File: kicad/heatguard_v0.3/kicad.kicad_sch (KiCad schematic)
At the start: 31 parts, among them J1 Conn_02x02_Odd_Even, J20 Conn_01x01, J7 Conn_01x12, J8 Conn_02x04_Odd_Even, J9 Conn_02x04_Odd_Even, U1 LM75B, U2 LM75B, U3 M24C02-FMN, U4 XIAO-RP2040-DIP

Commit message: Changes v0.2 -> v0.3 A
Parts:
- added Logo_open_hardware101: Logo_Open_Hardware_Small, Symbol:OSHW-Logo2_9.8x8mm_SilkScreen, symbol Graphic:Logo_Open_Hardware_Small
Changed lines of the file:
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@@
+	)
+	(symbol
+		(lib_id "Graphic:Logo_Open_Hardware_Small")
+		(at 182.88 261.62 0)
+		(unit 1)
+		(exclude_from_sim no)
+		(in_bom no)
+		(on_board yes)
+		(dnp no)
+		(fields_autoplaced yes)
+		(property "Reference" "Logo_open_hardware101"
+			(at 182.88 254.635 0)
+			(effects
+				(font
+					(size 1.27 1.27)
+				)
+				(hide yes)
+			)
+		)
+		(property "Value" "Logo_Open_Hardware_Small"
+			(at 182.88 267.335 0)
+			(effects
+				(font
+					(size 1.27 1.27)
+				)
+				(hide yes)
+			)
+		)
+		(property "Footprint" "Symbol:OSHW-Logo2_9.8x8mm_SilkScreen"
+			(at 182.88 261.62 0)
+			(effects
+				(font
+					(size 1.27 1.27)
+				)
+				(hide yes)
+			)
+		)
+		(property "Datasheet" "~"
+			(at 182.88 261.62 0)
+			(effects
+				(font
+					(size 1.27 1.27)
+				)
+				(hide yes)
+			)
+		)
+		(property "Description" "Open Hardware logo, small"
+			(at 182.88 261.62 0)
+			(effects
+				(font
+					(size 1.27 1.27)
+				)
+				(hide yes)
+			)
+		)
+		(instances
+			(project "kicad"
+				(path "/35c47459-45a7-4753-acae-c8b47e7575e1"
+					(reference "Logo_open_hardware101")
+					(unit 1)
+				)
+			)
+		)
 	)
 	(symbol

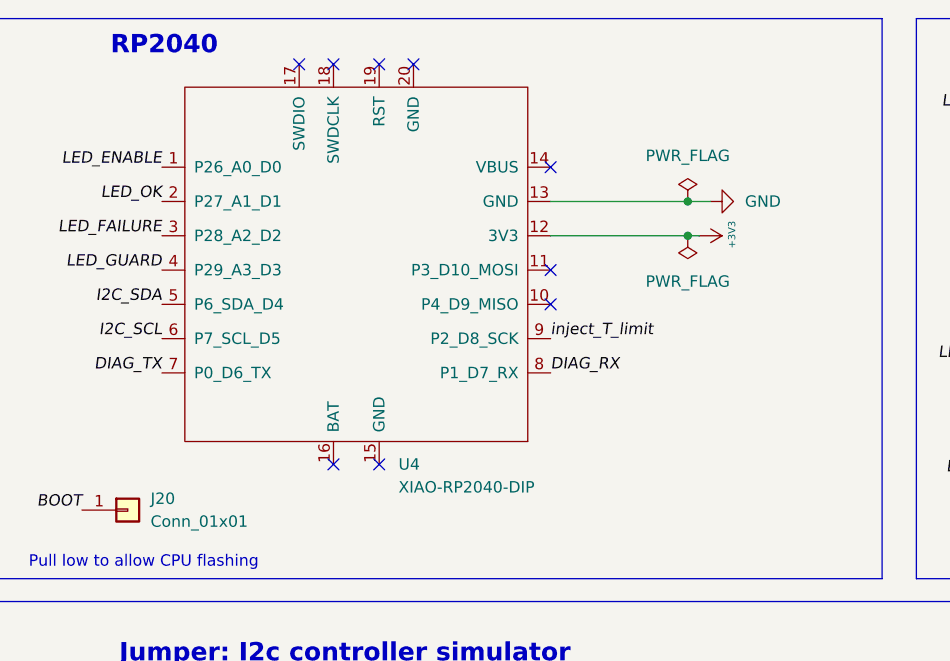
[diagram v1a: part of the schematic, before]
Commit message: Changes v0.2 -> v0.3 B: PCB: XIAO rp2040: Replace SMD with THT
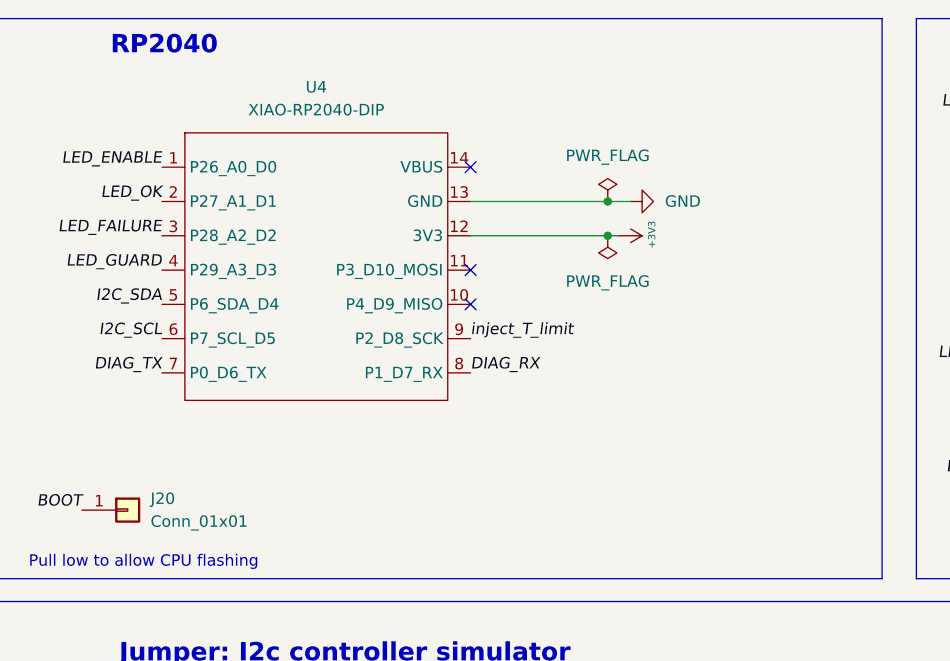
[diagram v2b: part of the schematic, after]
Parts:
- U4: footprint 00_project_library:XIAO-RP2040-SMD -> 00_project_library:XIAO-RP2040-DIP; symbol 00_project_library:XIAO-RP2040-SMD -> 00_project_library:XIAO-RP2040-DIP; now in the parts list
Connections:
- no-connect marks 18 -> 12
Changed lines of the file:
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@@
 	)
 	(junction
-		(at 99.06 39.37)
+		(at 90.17 39.37)
 		(diameter 0)
 		(color 0 0 0 0)
@@
 	)
 	(junction
-		(at 99.06 35.56)
+		(at 90.17 35.56)
 		(diameter 0)
 		(color 0 0 0 0)
@@
 	)
 	(no_connect
-		(at 83.82 43.18)
+		(at 74.93 43.18)
 	)
 	(no_connect
@@
 	)
 	(no_connect
-		(at 59.69 20.32)
-	)
-	(no_connect
 		(at 104.14 245.11)
 	)
@@
 	)
 	(no_connect
-		(at 64.77 64.77)
-	)
-	(no_connect
-		(at 68.58 20.32)
-	)
-	(no_connect
-		(at 59.69 64.77)
-	)
-	(no_connect
-		(at 55.88 20.32)
-	)
-	(no_connect
 		(at 104.14 240.03)
 	)
 	(no_connect
-		(at 83.82 31.75)
+		(at 74.93 31.75)
 	)
 	(no_connect
-		(at 83.82 46.99)
+		(at 74.93 46.99)
 	)
 	(no_connect
@@
 	)
 	(no_connect
-		(at 64.77 20.32)
-	)
-	(no_connect
 		(at 104.14 237.49)
 	)
@@
 	(wire
 		(pts
-			(xy 83.82 35.56) (xy 99.06 35.56)
+			(xy 74.93 35.56) (xy 90.17 35.56)
 		)
 		(stroke
@@
 	(wire
 		(pts
-			(xy 101.6 35.56) (xy 99.06 35.56)
+			(xy 92.71 35.56) (xy 90.17 35.56)
 		)
 		(stroke
@@
 	(wire
 		(pts
-			(xy 100.33 39.37) (xy 99.06 39.37)
+			(xy 91.44 39.37) (xy 90.17 39.37)
 		)
 		(stroke
@@
 	(wire
 		(pts
-			(xy 83.82 39.37) (xy 99.06 39.37)
+			(xy 74.93 39.37) (xy 90.17 39.37)
 		)
 		(stroke
@@
 	)
 	(label "inject_T_limit"
-		(at 83.82 50.8 0)
+		(at 74.93 50.8 0)
 		(effects
 			(font
@@
 	)
 	(label "DIAG_RX"
-		(at 83.82 54.61 0)
+		(at 74.93 54.61 0)
 		(effects
 			(font
@@
 	(symbol
 		(lib_id "power:+3V3")
-		(at 100.33 39.37 270)
+		(at 91.44 39.37 270)
 		(unit 1)
 		(exclude_from_sim no)
@@
 		(dnp no)
 		(property "Reference" "#PWR03"
-			(at 96.52 39.37 0)
+			(at 87.63 39.37 0)
 			(effects
 				(font
@@
 		)
 		(property "Value" "+3V3"
-			(at 103.9622 39.243 0)
+			(at 95.0722 39.243 0)
 			(effects
 				(font
@@
 		)
 		(property "Footprint" ""
-			(at 100.33 39.37 0)
+			(at 91.44 39.37 0)
 			(effects
 				(font
@@
 		)
 		(property "Datasheet" ""
-			(at 100.33 39.37 0)
+			(at 91.44 39.37 0)
 			(effects
 				(font
@@
 		)
 		(property "Description" "Power symbol creates a global label with name \"+3V3\""
-			(at 100.33 39.37 0)
+			(at 91.44 39.37 0)
 			(effects
 				(font
@@
 	(symbol
 		(lib_id "power:GND")
-		(at 101.6 35.56 90)
+		(at 92.71 35.56 90)
 		(unit 1)
 		(exclude_from_sim no)
@@
 		(fields_autoplaced yes)
 		(property "Reference" "#PWR04"
-			(at 107.95 35.56 0)
+			(at 99.06 35.56 0)
 			(effects
 				(font
@@
 		)
 		(property "Value" "GND"
-			(at 105.41 35.5599 90)
+			(at 96.52 35.5599 90)
 			(effects
 				(font
@@
 		)
 		(property "Footprint" ""
-			(at 101.6 35.56 0)
+			(at 92.71 35.56 0)
 			(effects
 				(font
@@
 		)
 		(property "Datasheet" ""
-			(at 101.6 35.56 0)
+			(at 92.71 35.56 0)
 			(effects
 				(font
@@
 		)
 		(property "Description" "Power symbol creates a global label with name \"GND\" , ground"
-			(at 101.6 35.56 0)
+			(at 92.71 35.56 0)
 			(effects
 				(font
@@
 	)
 	(symbol
-		(lib_id "00_project_library:XIAO-RP2040-SMD")
-		(at 62.23 43.18 0)
+		(lib_id "00_project_library:XIAO-RP2040-DIP")
+		(at 55.88 22.86 0)
 		(unit 1)
 		(exclude_from_sim no)
-		(in_bom no)
+		(in_bom yes)
 		(on_board yes)
 		(dnp no)
 		(fields_autoplaced yes)
 		(property "Reference" "U4"
-			(at 66.9133 64.77 0)
+			(at 57.785 22.86 0)
 			(effects
 				(font
 					(size 1.27 1.27)
 				)
-				(justify left)
 			)
 		)
 		(property "Value" "XIAO-RP2040-DIP"
-			(at 66.9133 67.31 0)
+			(at 57.785 25.4 0)
 			(effects
 				(font
 					(size 1.27 1.27)
 				)
-				(justify left)
 			)
 		)
-		(property "Footprint" "00_project_library:XIAO-RP2040-SMD"
-			(at 53.34 38.1 0)
+		(property "Footprint" "00_project_library:XIAO-RP2040-DIP"
+			(at 59.944 60.198 0)
 			(effects
 				(font
@@
 		)
 		(property "Datasheet" ""
-			(at 53.34 38.1 0)
+			(at 55.88 22.86 0)
 			(effects
 				(font
@@
 		)
 		(property "Description" ""
-			(at 62.23 43.18 0)
+			(at 55.88 22.86 0)
 			(effects
 				(font
@@
 		(pin "13"
 		)
-		(pin "18"
-		)
-		(pin "15"
-		)
-		(pin "19"
-		)
-		(pin "17"
-		)
-		(pin "16"
-		)
-		(pin "20"
-		)
 		(instances
 			(project ""
@@
 	(symbol
 		(lib_id "power:PWR_FLAG")
-		(at 99.06 35.56 0)
+		(at 90.17 35.56 0)
 		(unit 1)
 		(exclude_from_sim no)
@@
 		(fields_autoplaced yes)
 		(property "Reference" "#FLG0302"
-			(at 99.06 33.655 0)
+			(at 90.17 33.655 0)
 			(effects
 				(font
@@
 		)
 		(property "Value" "PWR_FLAG"
-			(at 99.06 30.48 0)
+			(at 90.17 30.48 0)
 			(effects
 				(font
@@
 		)
 		(property "Footprint" ""
-			(at 99.06 35.56 0)
+			(at 90.17 35.56 0)
 			(effects
 				(font
@@
 		)
 		(property "Datasheet" "~"
-			(at 99.06 35.56 0)
+			(at 90.17 35.56 0)
 			(effects
 				(font
@@
 		)
 		(property "Description" "Special symbol for telling ERC where power comes from"
-			(at 99.06 35.56 0)
+			(at 90.17 35.56 0)
 			(effects
 				(font
@@
 	(symbol
 		(lib_id "power:PWR_FLAG")
-		(at 99.06 39.37 180)
+		(at 90.17 39.37 180)
 		(unit 1)
 		(exclude_from_sim no)
@@
 		(fields_autoplaced yes)
 		(property "Reference" "#FLG01"
-			(at 99.06 41.275 0)
+			(at 90.17 41.275 0)
 			(effects
 				(font
@@
 		)
 		(property "Value" "PWR_FLAG"
-			(at 99.06 44.45 0)
+			(at 90.17 44.45 0)
 			(effects
 				(font
@@
 		)
 		(property "Footprint" ""
-			(at 99.06 39.37 0)
+			(at 90.17 39.37 0)
 			(effects
 				(font
@@
 		)
 		(property "Datasheet" "~"
-			(at 99.06 39.37 0)
+			(at 90.17 39.37 0)
 			(effects
 				(font
@@
 		)
 		(property "Description" "Special symbol for telling ERC where power comes from"
-			(at 99.06 39.37 0)
+			(at 90.17 39.37 0)
 			(effects
 				(font

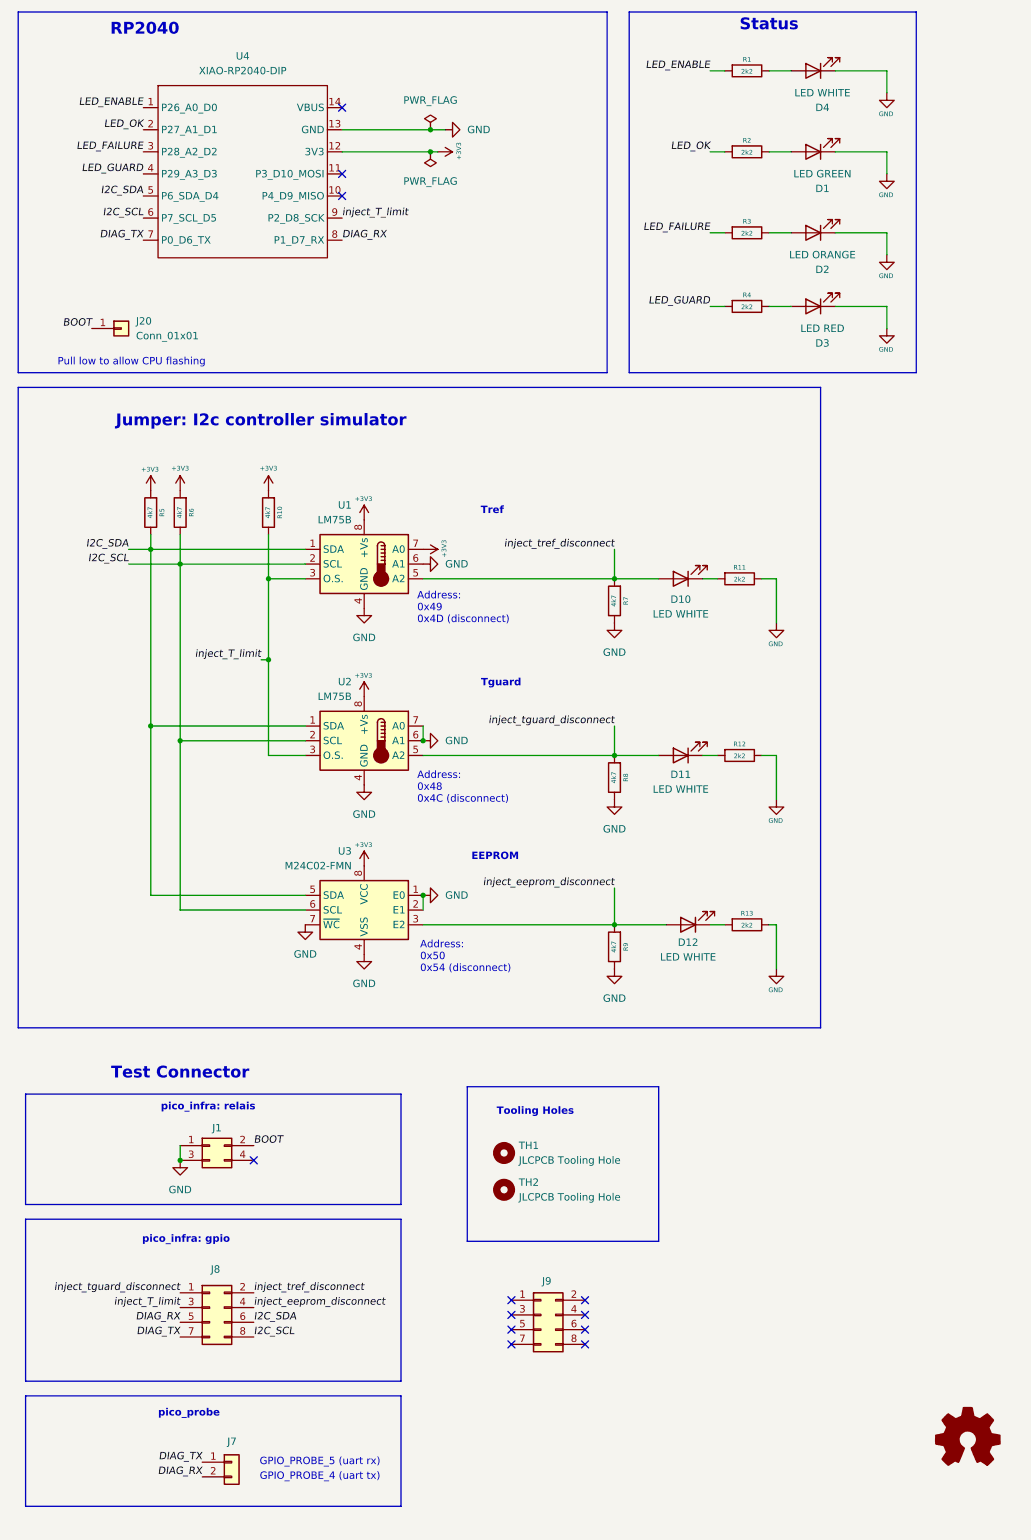
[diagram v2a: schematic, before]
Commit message: Changes v0.2 -> v0.3 C: Use relays in favor of GPIO
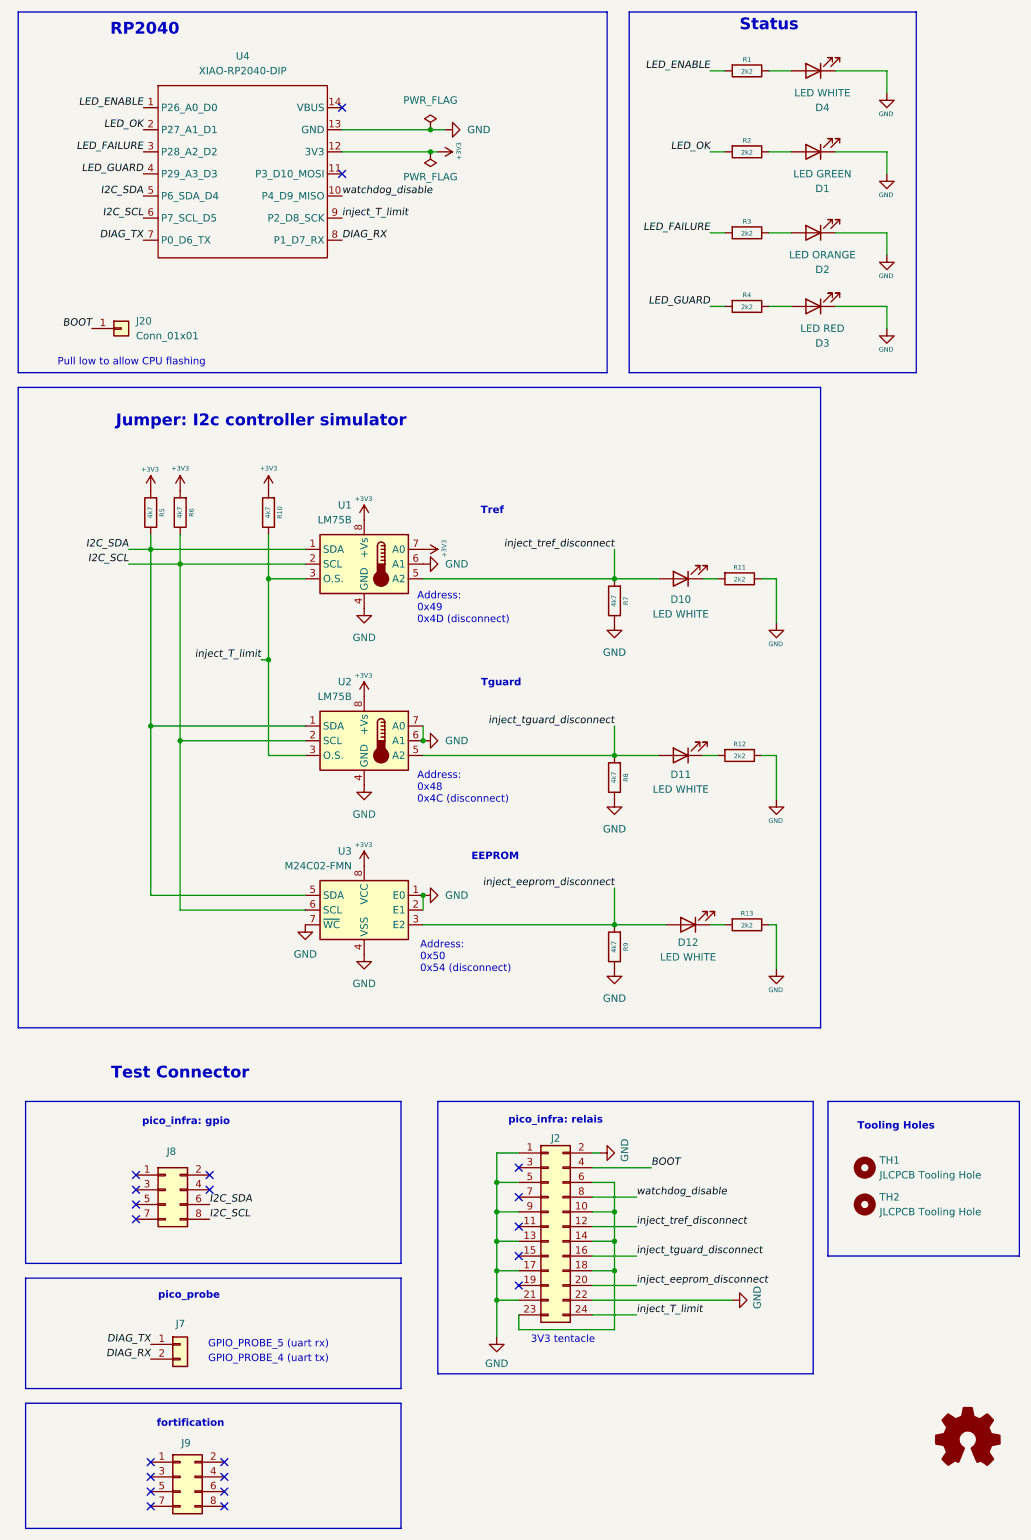
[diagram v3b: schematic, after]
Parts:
- removed J1: Conn_02x02_Odd_Even, 00_project_library:PinHeader_2x02_P2.54mm_Vertical_back, symbol Connector_Generic:Conn_02x02_Odd_Even
- added J2: Conn_02x12_Odd_Even, 00_project_library:PinHeader_2x12_P2.54mm_Vertical_back, symbol Connector_Generic:Conn_02x12_Odd_Even
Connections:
- net BOOT: now also J2.4 (Pin_4)
- net DIAG_RX: no longer J8.5 (Pin_5)
- net DIAG_TX: no longer J8.7 (Pin_7)
- net GND: now also J2.1 (Pin_1), J2.13 (Pin_13), J2.17 (Pin_17), J2.2 (Pin_2), J2.21 (Pin_21), J2.22 (Pin_22), J2.5 (Pin_5), J2.9 (Pin_9)
- net inject_T_limit: now also J2.24 (Pin_24); no longer J8.3 (Pin_3)
- net inject_eeprom_disconnect: now also J2.20 (Pin_20); no longer J8.4 (Pin_4)
- net inject_tguard_disconnect: now also J2.16 (Pin_16); no longer J8.1 (Pin_1)
- net inject_tref_disconnect: now also J2.12 (Pin_12); no longer J8.2 (Pin_2)
- net watchdog_disable: now reaches U4.10 (P4_D9_MISO)
- net watchdog_disable: now also J2.8 (Pin_8)
- new net: J2.10 (Pin_10), J2.14 (Pin_14), J2.18 (Pin_18), J2.23 (Pin_23), J2.6 (Pin_6)
- no-connect marks 12 -> 21
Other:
- note added: "3V3 tentacle"
- note added: "fortification"
- moved on the sheet: J7, J8, J9, TH1, TH2
